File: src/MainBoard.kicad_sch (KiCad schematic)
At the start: 74 parts, among them J10 Conn_01x01_Socket, J11 Conn_01x01_Socket, J12 Conn_01x01_Socket, J13 Conn_01x01_Socket, J14 Conn_01x01_Socket, J15 Conn_01x01_Socket, J16 Conn_01x01_Socket, J17 Conn_01x01_Socket, J18 Conn_01x01_Socket, J19 Conn_01x01_Socket, J2 MiniFit_2x11_F, J20 Conn_01x01_Socket, J21 Conn_01x01_Socket, J22 Conn_01x01_Socket, J23 Conn_01x01_Socket, J24 Conn_01x01_Socket, J25 Conn_01x01_Socket, J26 Conn_01x01_Socket, J27 Conn_01x01_Socket, J28 Conn_01x01_Socket, J29 Conn_01x01_Socket, J3 Conn_01x01_Socket, J30 Conn_01x01_Socket, J31 Conn_01x01_Socket, J32 Conn_01x01_Socket, J33 Conn_01x01_Socket, J34 Conn_01x01_Socket, J35 Conn_01x01_Socket, J36 Conn_01x01_Socket, J37 Conn_01x01_Socket, J38 Conn_01x01_Socket, J39 Conn_01x01_Socket, J4 Conn_01x01_Socket, J40 Conn_01x01_Socket, J5 Conn_01x01_Socket, J6 Conn_01x01_Socket, J7 Conn_01x01_Socket, J8 Conn_01x01_Socket, J9 Conn_01x01_Socket, K1 LEG-12, K2 LEG-12, Q1 2N7002, Q2 2N7002, Q3 2N7002, Q4 2N7002, Q5 2N7002, U1 LM555xN

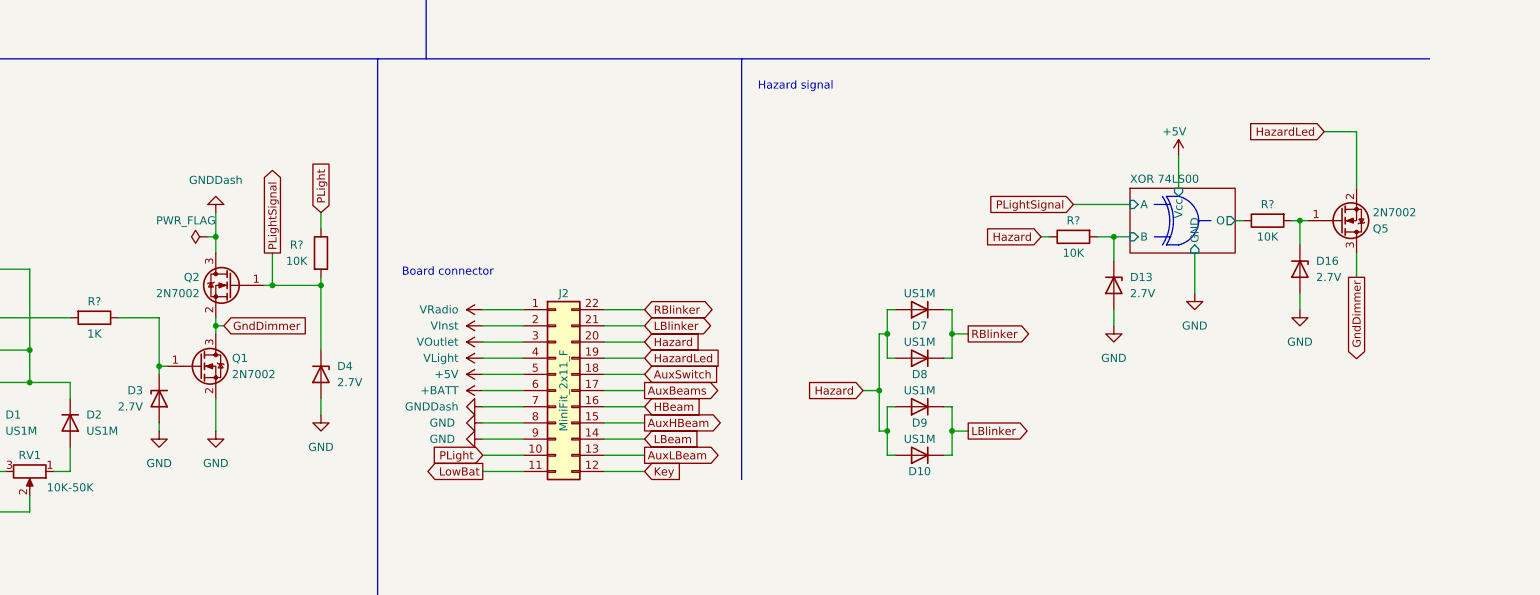
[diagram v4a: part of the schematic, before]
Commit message: Replace 7n2002 with IRLML0030 fo dimmer
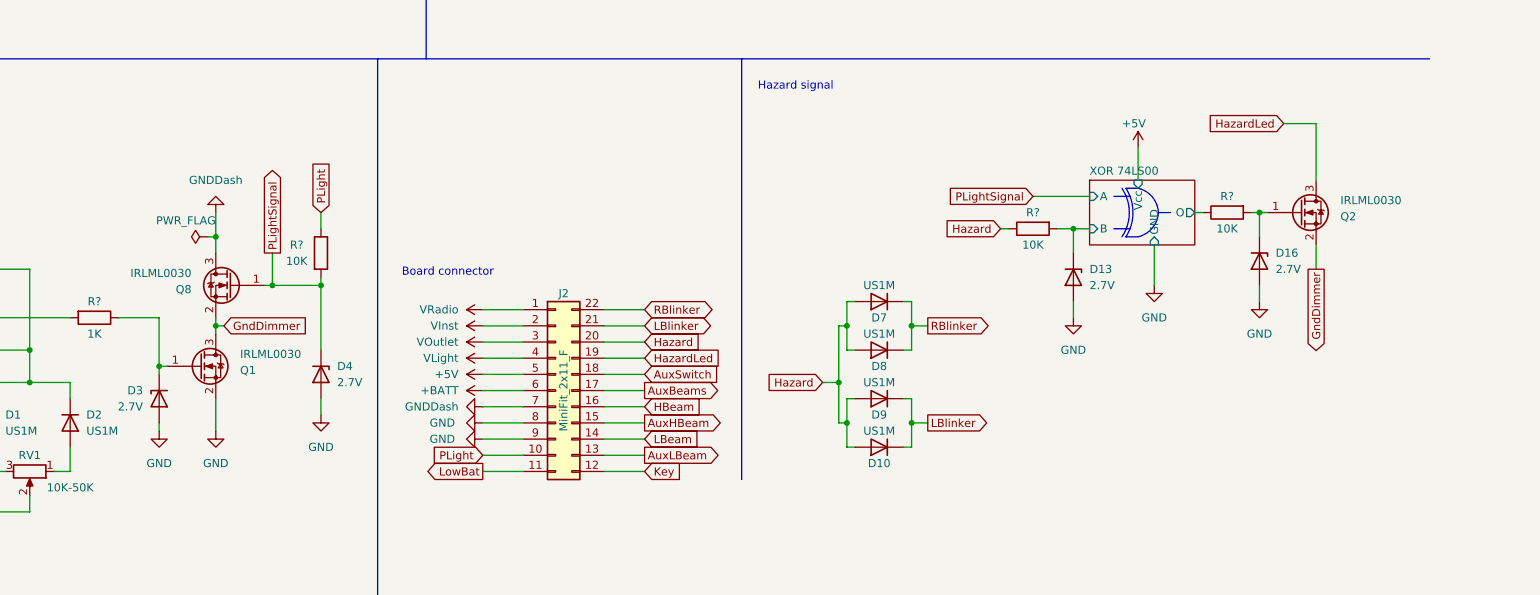
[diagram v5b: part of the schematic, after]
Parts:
- removed Q1, Q2, Q5: 2N7002, Package_TO_SOT_SMD:SOT-23, symbol Transistor_FET:2N7002
- added Q1, Q2, Q8: IRLML0030, Package_TO_SOT_SMD:SOT-23, symbol Transistor_FET:IRLML0030
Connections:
- net GND: now also Q1.2 (S)
- net GNDDash: now also Q8.3 (D)
- net GndDimmer: now also Q1.3 (D), Q2.2 (S), Q8.2 (S)
- net HazardLed: now also Q2.3 (D)
- net PLightSignal: now also Q8.1 (G)
- net at D16.1 (K), R?.2: now also Q2.1 (G)
- net at D3.1 (K), R?.1: now also Q1.1 (G)
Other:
- moved on the sheet: D10, D13, D16, D7, D8, D9, R?

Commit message: Update Design
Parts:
- removed Q1, Q2, Q8: IRLML0030, Package_TO_SOT_SMD:SOT-23, symbol Transistor_FET:IRLML0030
- added Q1, Q2, Q8: 2N7002, Package_TO_SOT_SMD:SOT-23, symbol Transistor_FET:2N7002
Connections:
- net GND: now also Q8.2 (S)
- net GNDDash: now also Q2.3 (D)
- net GndDimmer: now also Q1.2 (S), Q2.2 (S), Q8.3 (D)
- net HazardLed: now also Q1.3 (D)
- net PLightSignal: now also Q2.1 (G)
- net at D16.1 (K), R?.2: now also Q1.1 (G)
- net at D3.1 (K), R?.1: now also Q8.1 (G)

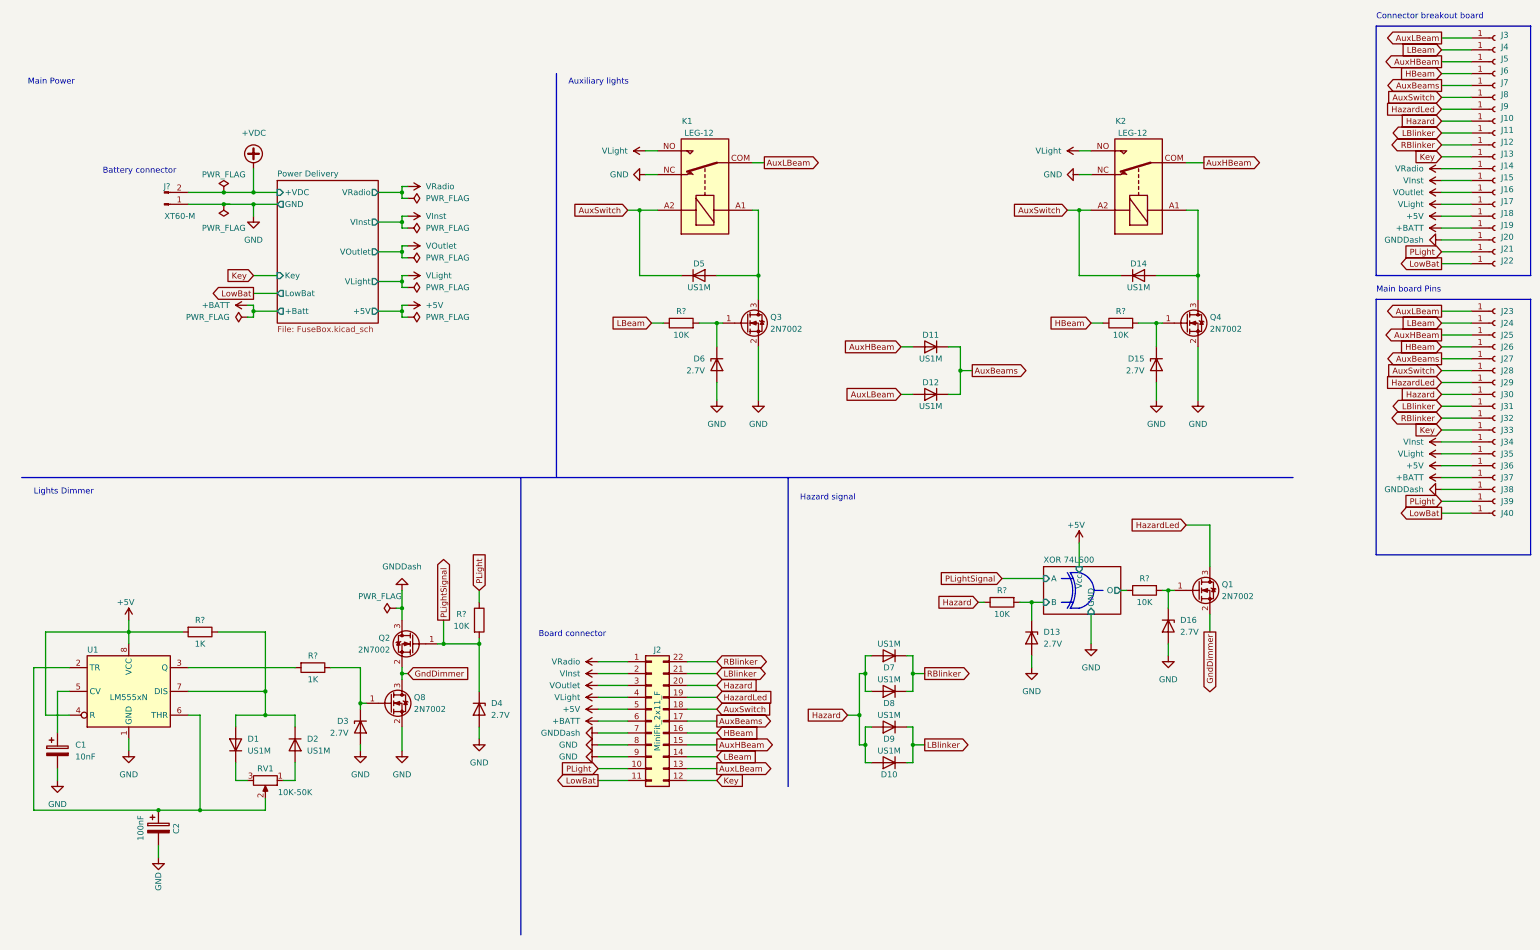
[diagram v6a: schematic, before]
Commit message: simplify circuit diagram. Remove unecessary features; Split board into two components|
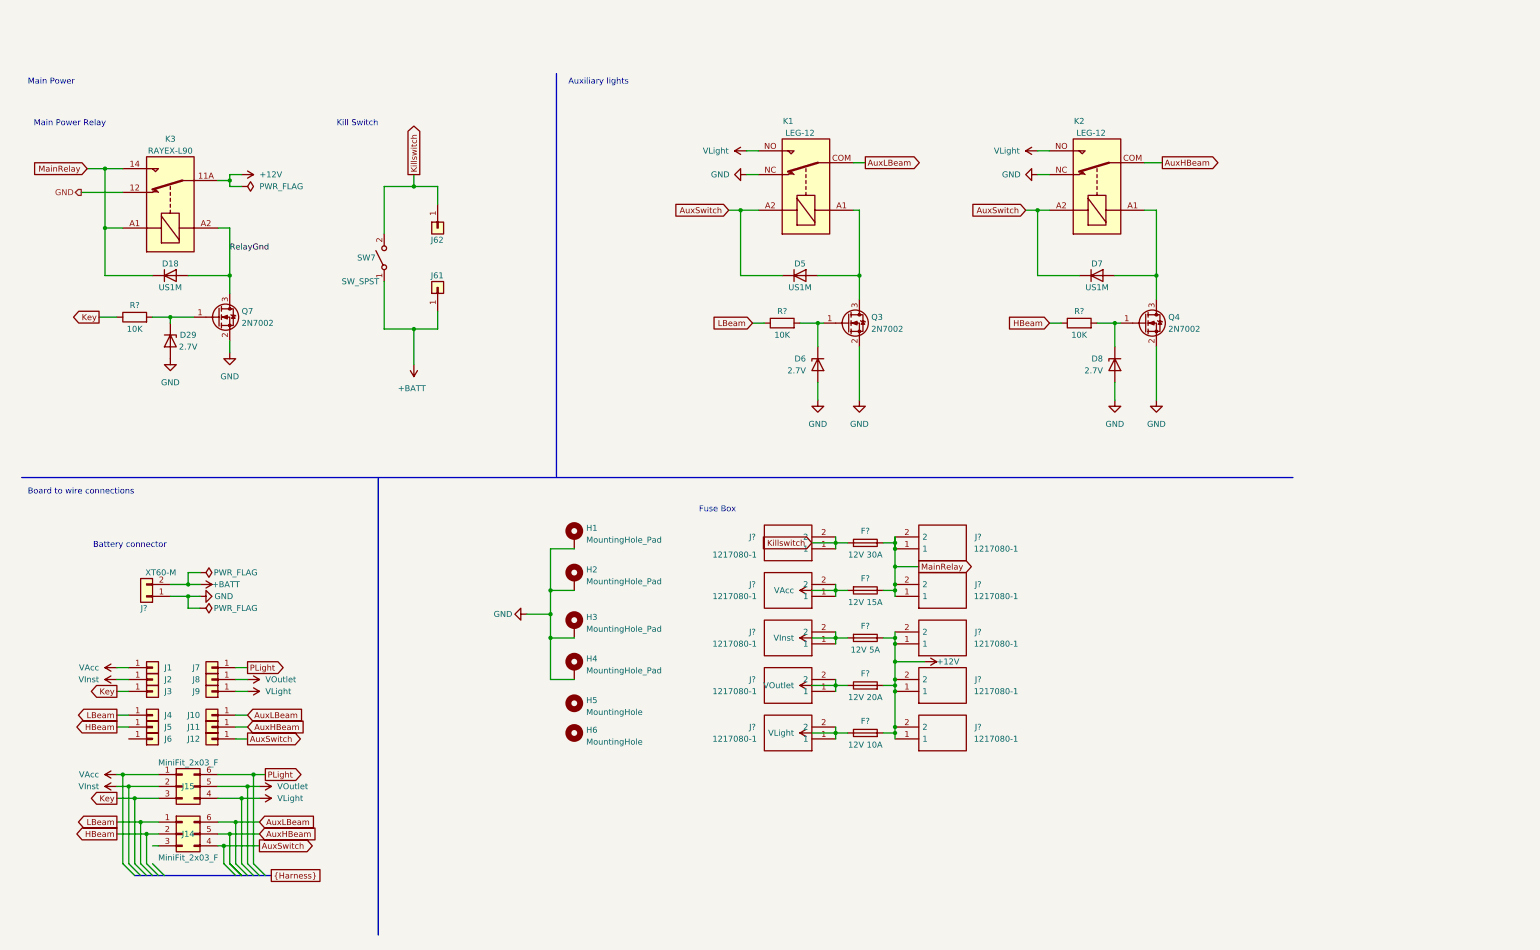
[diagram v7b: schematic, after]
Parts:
- removed C1: 10nF, symbol Device:C_Polarized
- removed C2: 100nF, symbol Device:C_Polarized
- removed D1, D10, D11, D12, D2, D7, D8, D9: US1M, Diode_SMD:D_SMA, symbol Diode:US1M
- removed D13, D16, D3, D4: 2.7V, Diode_SMD:D_MiniMELF, symbol Diode:BZV55C2V7
- removed J10, J11, J12, J13, J14, J15, J16, J17, J18, J19, J20, J21, J22, J23, J24, J25, J26, J27, J28, J29, J3, J30, J31, J32, J33, J34, J35, J36, J37, J38, J39, J4, J40, J5, J6, J7, J8, J9: Conn_01x01_Socket, Connector_Pin:Pin_D1.0mm_L10.0mm, symbol Connector:Conn_01x01_Socket
- removed J2: MiniFit_2x11_F, symbol Connector_Generic:Conn_02x11_Counter_Clockwise
- removed J?: XT60-M, Local Footprints:AMASS_XT60PW-M_1x02_P7.20mm_Horizontal_Short, symbol Connector:Conn_01x02_Pin
- removed Q1, Q2, Q8: 2N7002, Package_TO_SOT_SMD:SOT-23, symbol Transistor_FET:2N7002
- removed R? (x2): 1K, Resistor_SMD:R_1206_3216Metric_Pad1.30x1.75mm_HandSolder, symbol Device:R
- removed R? (x3): 10K, Resistor_SMD:R_1206_3216Metric_Pad1.30x1.75mm_HandSolder, symbol Device:R
- removed RV1: 10K-50K, symbol Device:R_Potentiometer
- removed U1: LM555xN, Package_DIP:DIP-8_W7.62mm_Socket_LongPads, symbol Timer:LM555xN
- added D18: US1M, Diode_SMD:D_SMA, symbol Diode:US1M
- added D29: 2.7V, Diode_THT:D_DO-35_SOD27_P7.62mm_Horizontal, symbol Diode:BZV55C2V7
- added F?: 12V 20A, symbol Device:Fuse
- added F?: 12V 30A, symbol Device:Fuse
- added F?: 12V 5A, symbol Device:Fuse
- added F?: 12V 15A, symbol Device:Fuse
- added F?: 12V 10A, symbol Device:Fuse
- added H1, H2, H3, H4: MountingHole_Pad, MountingHole:MountingHole_3.2mm_M3_DIN965_Pad, symbol Mechanical:MountingHole_Pad
- added H5, H6: MountingHole, MountingHole:MountingHole_5.3mm_M5_Pad_Via, symbol Mechanical:MountingHole
- added J1, J10, J11, J12, J2, J3, J4, J5, J6, J7, J8, J9: Conn_01x01, TestPoint:TestPoint_THTPad_D2.5mm_Drill1.2mm, symbol Connector_Generic:Conn_01x01
- added J14, J15: MiniFit_2x03_F, symbol Connector_Generic:Conn_02x03_Counter_Clockwise
- added J61, J62: Conn_01x01, MountingHole:MountingHole_3.2mm_M3_DIN965_Pad, symbol Connector_Generic:Conn_01x01
- added J? (x10): 1217080-1, 1217080-1, symbol SamacSys_Parts:1217080-1
- added J?: XT60-M, Local Footprints:AMASS_XT60PW-M_1x02_P7.20mm_Horizontal_Short, symbol Connector_Generic:Conn_01x02
- added K3: RAYEX-L90, Local Footprints:Relay_SPDT_RAYEX-L90, symbol Relay:RAYEX-L90
- added Q7: 2N7002, Package_TO_SOT_SMD:SOT-23, symbol Transistor_FET:2N7002
- added R?: 10K, Resistor_SMD:R_1206_3216Metric_Pad1.30x1.75mm_HandSolder, symbol Device:R
- added SW7: SW_SPST, symbol Switch:SW_SPST
- D6: footprint Diode_SMD:D_MiniMELF -> Diode_THT:D_DO-35_SOD27_P7.62mm_Horizontal
- D8: renamed from D15; footprint Diode_SMD:D_MiniMELF -> Diode_THT:D_DO-35_SOD27_P7.62mm_Horizontal
- renumbered D14 to D7
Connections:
- net +BATT: now also J61.1 (Pin_1), J?.2 (Pin_2), SW7.1 (A)
- net AuxHBeam: now also J11.1 (Pin_1), J15.5 (Pin_5)
- net AuxLBeam: now also J10.1 (Pin_1), J15.6 (Pin_6)
- net AuxSwitch: now also J12.1 (Pin_1), J15.4 (Pin_4)
- net GND: now also D29.2 (A), H1.1, H2.1, H3.1, H4.1, J?.1 (Pin_1), K3.12, Q7.2 (S)
- net HBeam: now also J15.2 (Pin_2), J5.1 (Pin_1)
- net Key: now also J14.3 (Pin_3), J3.1 (Pin_1), R?.1
- net LBeam: now also J15.1 (Pin_1), J4.1 (Pin_1)
- net PLight: now also J14.6 (Pin_6), J7.1 (Pin_1)
- net VInst: now also F?.2, J14.2 (Pin_2), J2.1 (Pin_1), J?.1, J?.2
- net VLight: now also F?.1, J14.4 (Pin_4), J9.1 (Pin_1), J?.1, J?.2
- net VOutlet: now also F?.1, J14.5 (Pin_5), J8.1 (Pin_1), J?.1, J?.2
- new net: D29.1 (K), Q7.1 (G), R?.2
- new net +12V: F?.1, F?.2, F?.2, J?.1, J?.1, J?.1, J?.2, J?.2, J?.2, K3.11A, K3.11B
- new net Killswitch: F?.2, J62.1 (Pin_1), J?.1, J?.2, SW7.2 (B)
- new net MainRelay: D18.1 (K), F?.1, F?.1, J?.1, J?.1, J?.2, J?.2, K3.14, K3.A1
- new net RelayGnd: D18.2 (A), K3.A2, Q7.3 (D)
- new net VAcc: F?.2, J1.1 (Pin_1), J14.1 (Pin_1), J?.1, J?.2
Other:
- removed sheet Power Delivery
- removed sheet XOR 74LS00
- note added: "Board to wire connections"
- note added: "Fuse Box"
- note added: "Kill Switch"
- note added: "Main Power Relay"
- note removed: "Board connector"
- note removed: "Connector breakout board"
- note removed: "Hazard signal"
- note removed: "Lights Dimmer"
- note removed: "Main board Pins"
- moved on the sheet: D5, D6, D7, D8, K1, K2, Q3, Q4, R?

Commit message: Simplify circuit diagram. Remove unecessary features
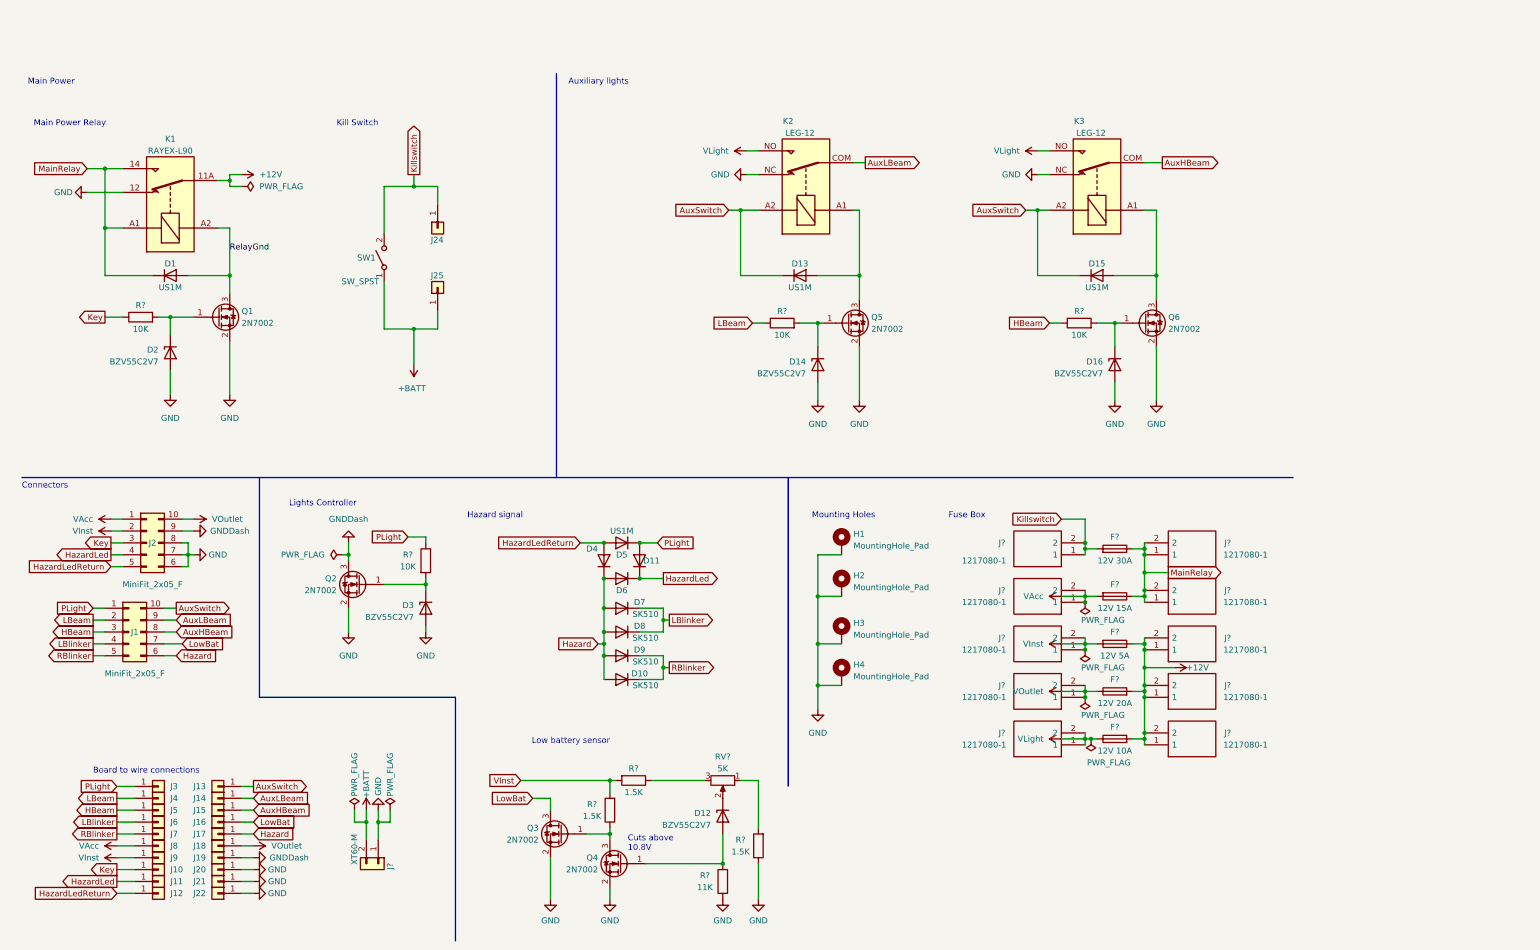
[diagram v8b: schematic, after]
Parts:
- removed D29, D6, D8: 2.7V, Diode_THT:D_DO-35_SOD27_P7.62mm_Horizontal, symbol Diode:BZV55C2V7
- removed H5, H6: MountingHole, MountingHole:MountingHole_5.3mm_M5_Pad_Via, symbol Mechanical:MountingHole
- removed J14, J15: MiniFit_2x03_F, symbol Connector_Generic:Conn_02x03_Counter_Clockwise
- removed J3: Conn_01x01, TestPoint:TestPoint_THTPad_D2.5mm_Drill1.2mm, symbol Connector_Generic:Conn_01x01
- added D10, D7, D8, D9: SK510, Diode_SMD:D_SMC_Handsoldering, symbol Device:D
- added D11, D4, D5, D6: US1M, Diode_SMD:D_SMA_Handsoldering, symbol Diode:US1M
- added D12, D14, D16, D2, D3: BZV55C2V7, Diode_SMD:D_MiniMELF_Handsoldering, symbol Diode:BZV55C2V7
- added J1, J2: MiniFit_2x05_F, Connector_Molex:Molex_Mini-Fit_Jr_5566-10A_2x05_P4.20mm_Vertical, symbol Connector_Generic:Conn_02x05_Counter_Clockwise
- added J12, J14, J15, J16, J17, J20, J21, J22, J5: Conn_01x01, TestPoint:TestPoint_THTPad_D2.5mm_Drill1.2mm, symbol Connector_Generic:Conn_01x01
- added Q2, Q3, Q4: 2N7002, Package_TO_SOT_SMD:SOT-23, symbol Transistor_FET:2N7002
- added R?: 11K, Resistor_SMD:R_1206_3216Metric_Pad1.30x1.75mm_HandSolder, symbol Device:R
- added R? (x3): 1.5K, Resistor_SMD:R_1206_3216Metric_Pad1.30x1.75mm_HandSolder, symbol Device:R
- added R?: 10K, Resistor_SMD:R_1206_3216Metric_Pad1.30x1.75mm_HandSolder, symbol Device:R
- added RV?: 5K, Potentiometer_THT:Potentiometer_Piher_PT-15-V02_Vertical, symbol Device:R_Potentiometer
- D1: renamed from D18; footprint Diode_SMD:D_SMA -> Diode_SMD:D_SMA_Handsoldering
- D13: renamed from D5; footprint Diode_SMD:D_SMA -> Diode_SMD:D_SMA_Handsoldering
- D15: renamed from D7; footprint Diode_SMD:D_SMA -> Diode_SMD:D_SMA_Handsoldering
- renumbered J12 to J13, J8 to J18, J9 to J19, J62 to J24, J61 to J25, J5 to J3, J1 to J8, J2 to J9, K3 to K1, K1 to K2, K2 to K3, Q7 to Q1, Q3 to Q5, Q4 to Q6, SW7 to SW1
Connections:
- net AuxHBeam: now also J1.8 (Pin_8), J15.1 (Pin_1); no longer J11.1 (Pin_1)
- net AuxLBeam: now also J1.9 (Pin_9), J14.1 (Pin_1); no longer J10.1 (Pin_1)
- net AuxSwitch: now also J1.10 (Pin_10)
- net GND: now also D14.2 (A), D16.2 (A), D2.2 (A), D3.2 (A), J2.6 (Pin_6), J2.7 (Pin_7), J2.8 (Pin_8), J20.1 (Pin_1), J21.1 (Pin_1), J22.1 (Pin_1), Q2.2 (S), Q3.2 (S), Q4.2 (S), R?.1, R?.1
- net HBeam: now also J1.3 (Pin_3), J5.1 (Pin_1); no longer J3.1 (Pin_1)
- net Key: now also J10.1 (Pin_1), J2.3 (Pin_3)
- net LBeam: now also J1.2 (Pin_2)
- net PLight: now also J3.1 (Pin_1), D11.2 (A), D5.1 (K), J1.1 (Pin_1), R?.1; no longer J7.1 (Pin_1)
- net VAcc: now also J2.1 (Pin_1)
- net VInst: now also J2.2 (Pin_2), R?.2, R?.2
- net VLight: no longer J19.1 (Pin_1)
- net VOutlet: now also J2.10 (Pin_10)
- net at Q1.1 (G), R?.2: now also D2.1 (K)
- net LBlinker: now reaches J6.1 (Pin_1)
- net LBlinker: now also D7.1 (K), D8.1 (K), J1.4 (Pin_4)
- net at Q6.1 (G), R?.2: now also D16.1 (K)
- net at Q5.1 (G), R?.2: now also D14.1 (K)
- new net: D12.2 (A), Q4.1 (G), R?.2
- new net: Q3.1 (G), Q4.3 (D), R?.1
- new net: R?.2, RV?.1
- new net: D12.1 (K), RV?.2
- new net: R?.1, RV?.3
- new net: D3.1 (K), Q2.1 (G), R?.2
- new net GNDDash: J19.1 (Pin_1), J2.9 (Pin_9), Q2.3 (D)
- new net Hazard: D10.2 (A), D4.1 (K), D6.2 (A), D7.2 (A), D8.2 (A), D9.2 (A), J1.6 (Pin_6), J17.1 (Pin_1)
- new net HazardLed: D11.1 (K), D6.1 (K), J11.1 (Pin_1), J2.4 (Pin_4)
- new net HazardLedReturn: D4.2 (A), D5.2 (A), J12.1 (Pin_1), J2.5 (Pin_5)
- new net LowBat: J1.7 (Pin_7), J16.1 (Pin_1), Q3.3 (D)
- new net RBlinker: D10.1 (K), D9.1 (K), J1.5 (Pin_5), J7.1 (Pin_1)
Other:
- note added: "Connectors"
- note added: "Cuts above 10.8V"
- note added: "Hazard signal"
- note added: "Lights Controller"
- note added: "Low battery sensor"
- note added: "Mounting Holes"
- note removed: "Battery connector"
- moved on the sheet: F?, H1, H2, H3, H4, J13, J18, J19, J3, J8, J9, J?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
